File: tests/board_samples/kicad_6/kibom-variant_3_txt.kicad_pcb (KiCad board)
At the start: 2 copper layers, 12.7 x 13.6 mm, 6 parts

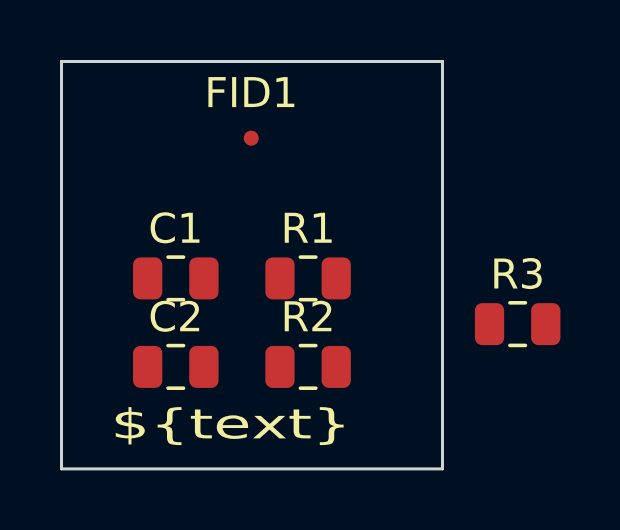
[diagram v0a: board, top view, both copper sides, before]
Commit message: Fixed (KiCad 6) traces not visible in 3D render
Fixes #177
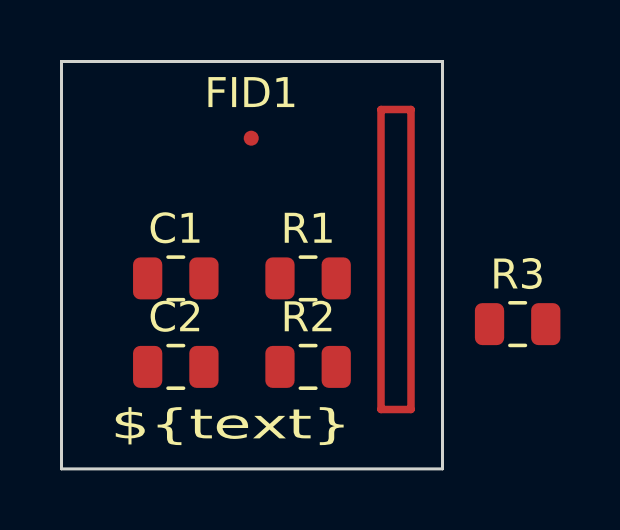
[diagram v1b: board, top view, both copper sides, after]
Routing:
- net (no net): track 0.00 -> 22.0 mm
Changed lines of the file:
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@@
     )
   )
+  (property "text" "Test")
   (net 0 "")
   (net 1 "Net-(C1-Pad2)")
@@
     (effects (font (size 1.5 1.5) (thickness 0.3)))
   )
+  (segment (start 145 82) (end 145 92) (width 0.25) (layer "F.Cu") (net 0))
+  (segment (start 145 92) (end 144 92) (width 0.25) (layer "F.Cu") (net 0))
+  (segment (start 144 92) (end 144 82) (width 0.25) (layer "F.Cu") (net 0))
+  (segment (start 144 82) (end 145 82) (width 0.25) (layer "F.Cu") (net 0))
 )
